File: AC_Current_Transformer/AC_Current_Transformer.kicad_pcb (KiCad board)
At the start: 2 copper layers, 19.5 x 16 mm, 6 parts, among them J101 Interface, J102 AudioJack3

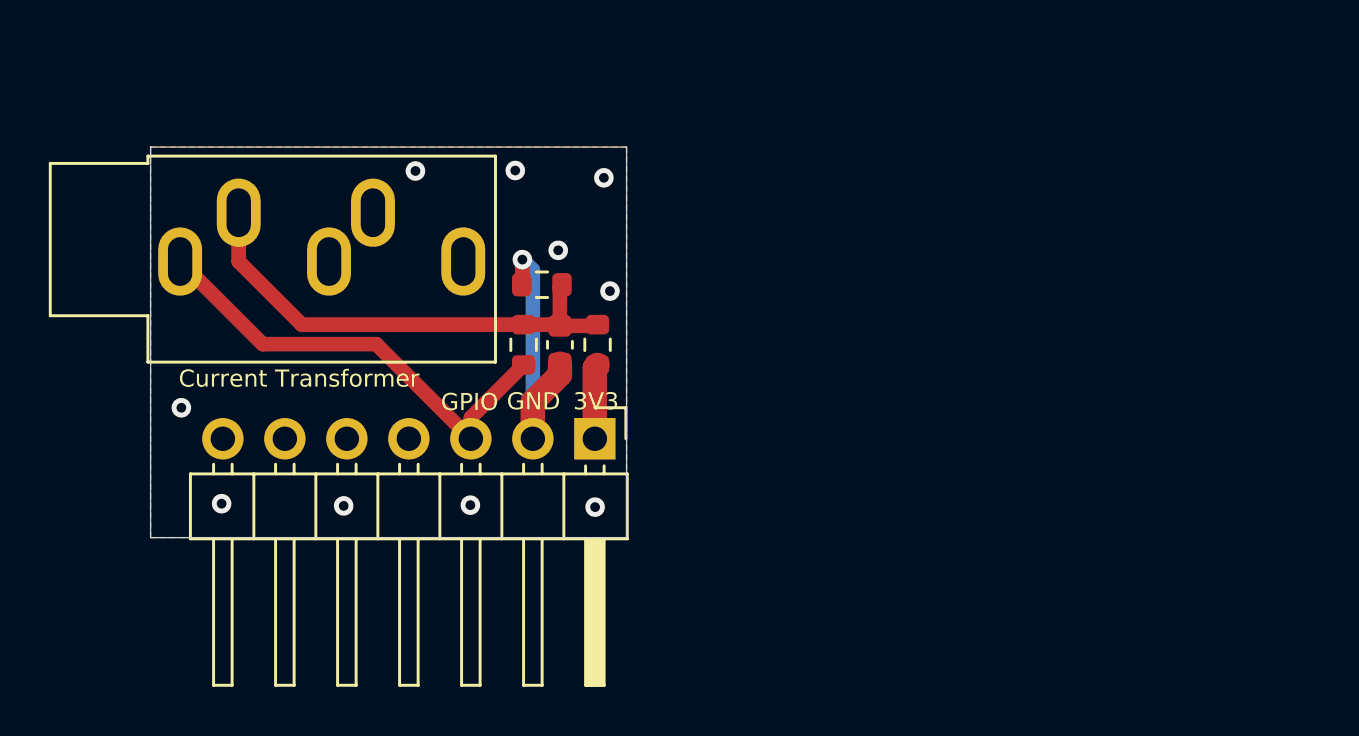
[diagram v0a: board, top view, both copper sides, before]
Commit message: Standardize on 20mm x 20mm boards with 7pin header
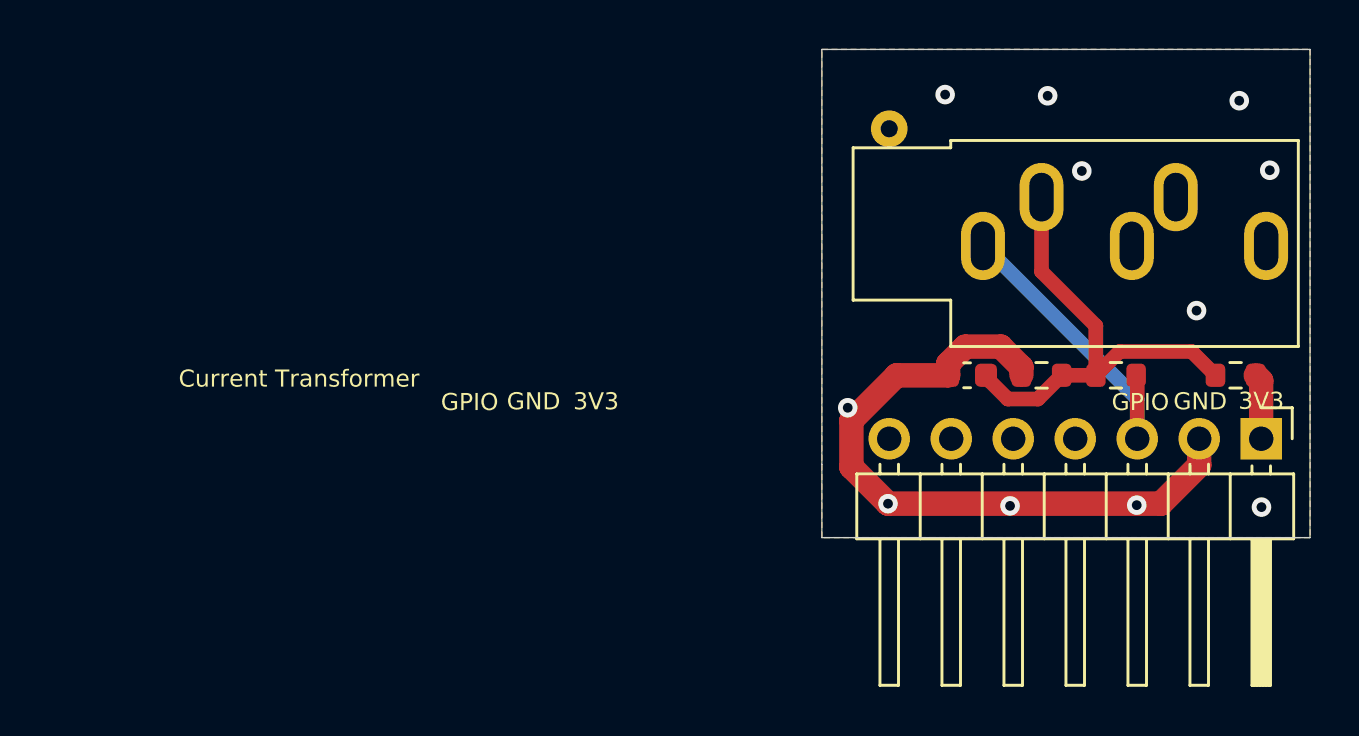
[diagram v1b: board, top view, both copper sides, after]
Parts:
- added REF**: TestPoint_THTPad_D1.5mm_Drill0.7mm, TestPoint:TestPoint_THTPad_D1.5mm_Drill0.7mm, F.Cu at (150.8, 76.2)
- moved J102 32.9 mm to (154.6, 81.0)
- moved J101 27.3 mm to (166.0, 89.0)
- moved R102 26.2 mm to (164.9, 86.3), turned to 180 degrees
- moved R101 24.3 mm to (160.1, 86.3), turned to 180 degrees
- moved R103 20.8 mm to (157.0, 86.3)
- moved C101 16.7 mm to (153.9, 86.3), turned to 180 degrees
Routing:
- net GND: track 12.1 -> 27.7 mm
- net /GPIO: track 18.8 -> 13.2 mm
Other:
- board size 19.5 x 16 mm -> 20 x 20 mm
- board text added: "Hole here is for Single pin to support board edge if needed for connectors when Horizontal on SH-ESP32"

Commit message: New GND Pin.  Added PI Filters to all inputs.    Refined Layout
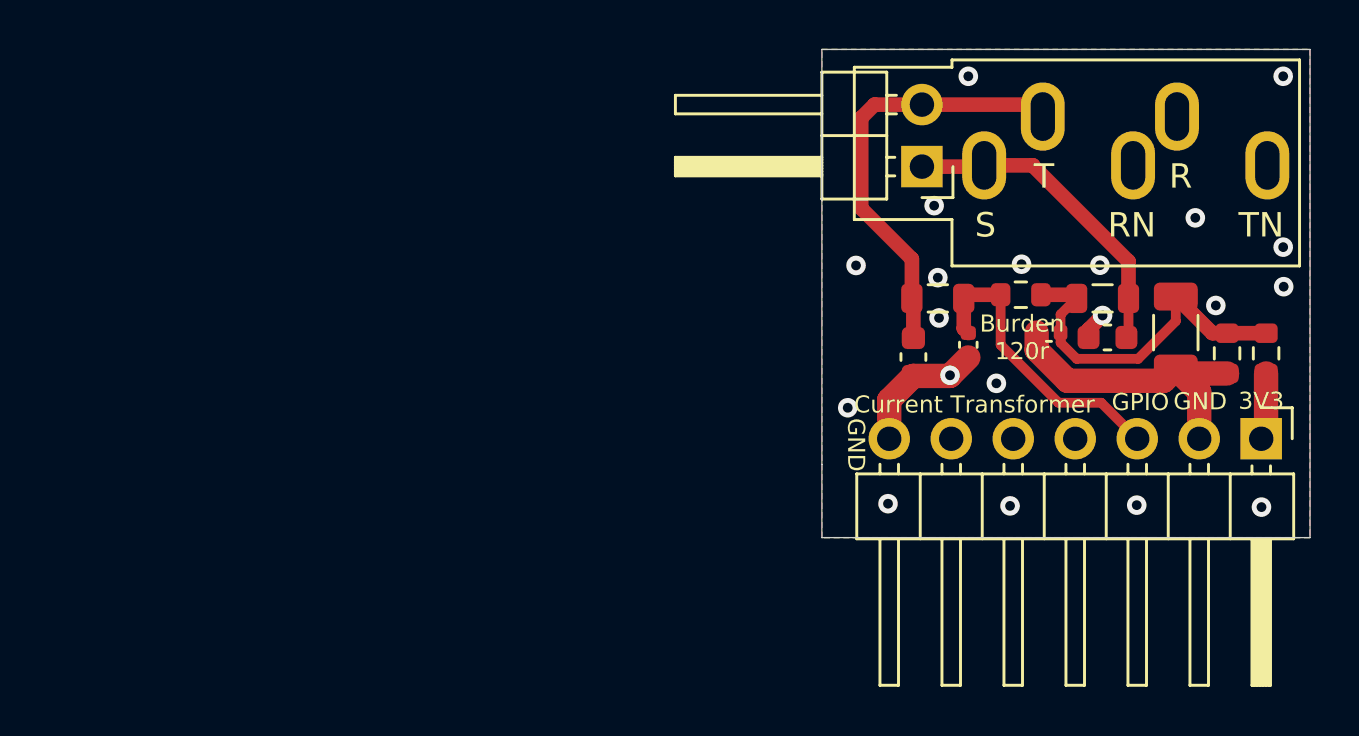
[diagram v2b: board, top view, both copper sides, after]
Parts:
- removed REF**: TestPoint_THTPad_D1.5mm_Drill0.7mm, TestPoint:TestPoint_THTPad_D1.5mm_Drill0.7mm
- added C102: 33pF, Capacitor_SMD:C_0402_1005Metric, F.Cu at (157.3, 84.6)
- added C103: 33pF, Capacitor_SMD:C_0402_1005Metric, F.Cu at (154.0, 85.1)
- added C104: 33pF/50V, Capacitor_SMD:C_0603_1608Metric, F.Cu at (151.8, 85.6)
- added C105: 33pF/50V, Capacitor_SMD:C_0603_1608Metric, F.Cu at (159.7, 84.8)
- added FB101: GZ2012D101TF, Inductor_SMD:L_0805_2012Metric, F.Cu at (152.8, 83.2)
- added FB102: GZ2012D101TF, Inductor_SMD:L_0805_2012Metric, F.Cu at (159.5, 83.2)
- added J103: Conn_01x02, Connector_PinHeader_2.54mm:PinHeader_1x02_P2.54mm_Horizontal, F.Cu at (152.1, 77.8)
- C101: value CP -> 10uf/50V; footprint Capacitor_SMD:C_0603_1608Metric -> Capacitor_SMD:C_1206_3216Metric
- R102, R103: value 12 -> 10k
- moved C101 8.73 mm to (162.5, 84.6), turned to 270 degrees
- moved R103 7.65 mm to (164.6, 85.5), turned to 270 degrees
- moved R101 5.11 mm to (156.2, 83.0), turned to 0 degrees
- moved J102 3.30 mm to (154.7, 77.8)
- moved R102 1.54 mm to (166.2, 85.5), turned to 90 degrees
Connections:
- J101 pad 7: (no net) -> GND
- J102 pad S: /GPIO -> Net-(C105-Pad1)
- J102 pad T: Net-(C101-Pad1) -> Net-(C104-Pad1)
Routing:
- net Net-(C104-Pad1): track 0.00 -> 18.2 mm
- net Net-(C105-Pad1): track 0.00 -> 13.8 mm
- net GND: track 27.7 -> 19.3 mm, vias 11 -> 20
- net Net-(C101-Pad1): track 19.3 -> 14.9 mm
- net /GPIO: track 13.2 -> 12.3 mm
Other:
- board text added: "Burden 120r"
- board text added: "R"
- board text added: "RN"
- board text added: "S"
- board text added: "T"
- board text added: "TN"
